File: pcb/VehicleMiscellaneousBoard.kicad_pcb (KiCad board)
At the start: 4 copper layers, 50 x 50 mm, 5 parts, among them J1 Conn_02x05_Top_Bottom, U1 OpenMV H7+, U2 Seeed_Studio_XIAO-ESP32-S3-Se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

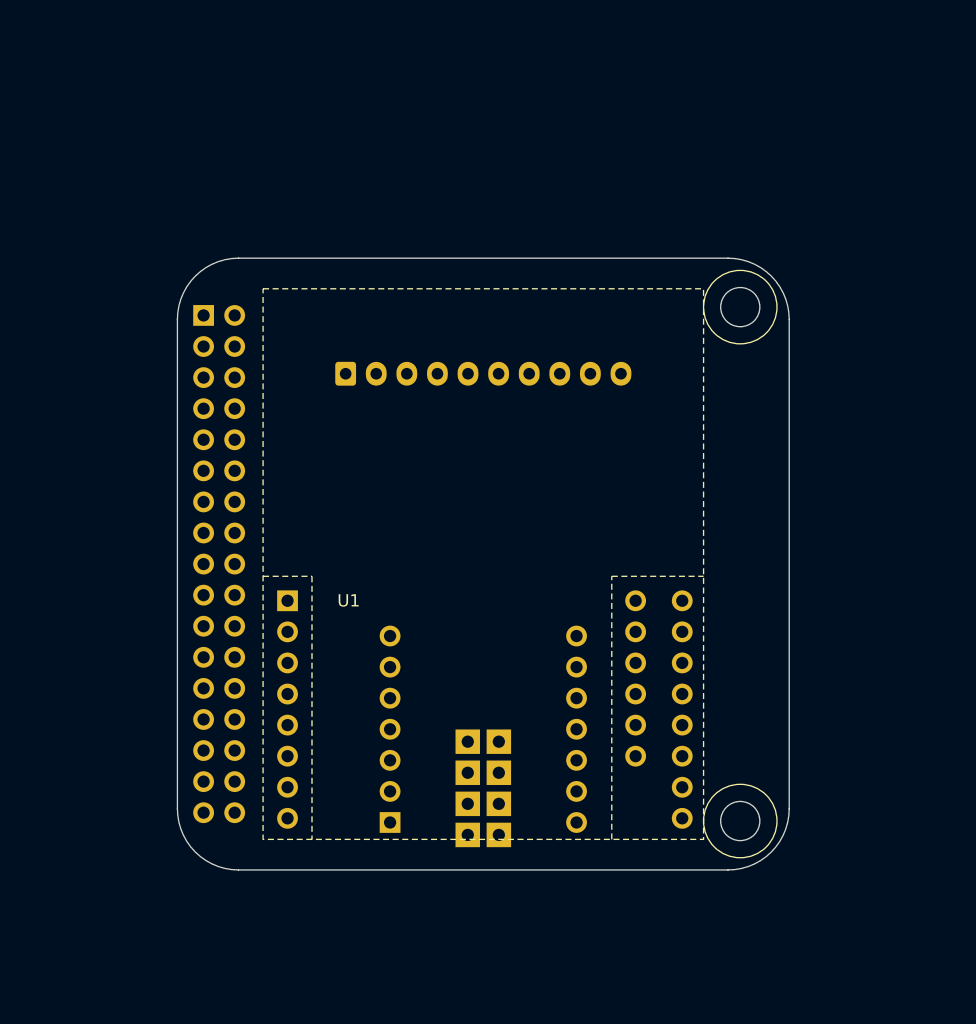
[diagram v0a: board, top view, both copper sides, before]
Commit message: Routed `VehicleMiscellaneousBoard`.
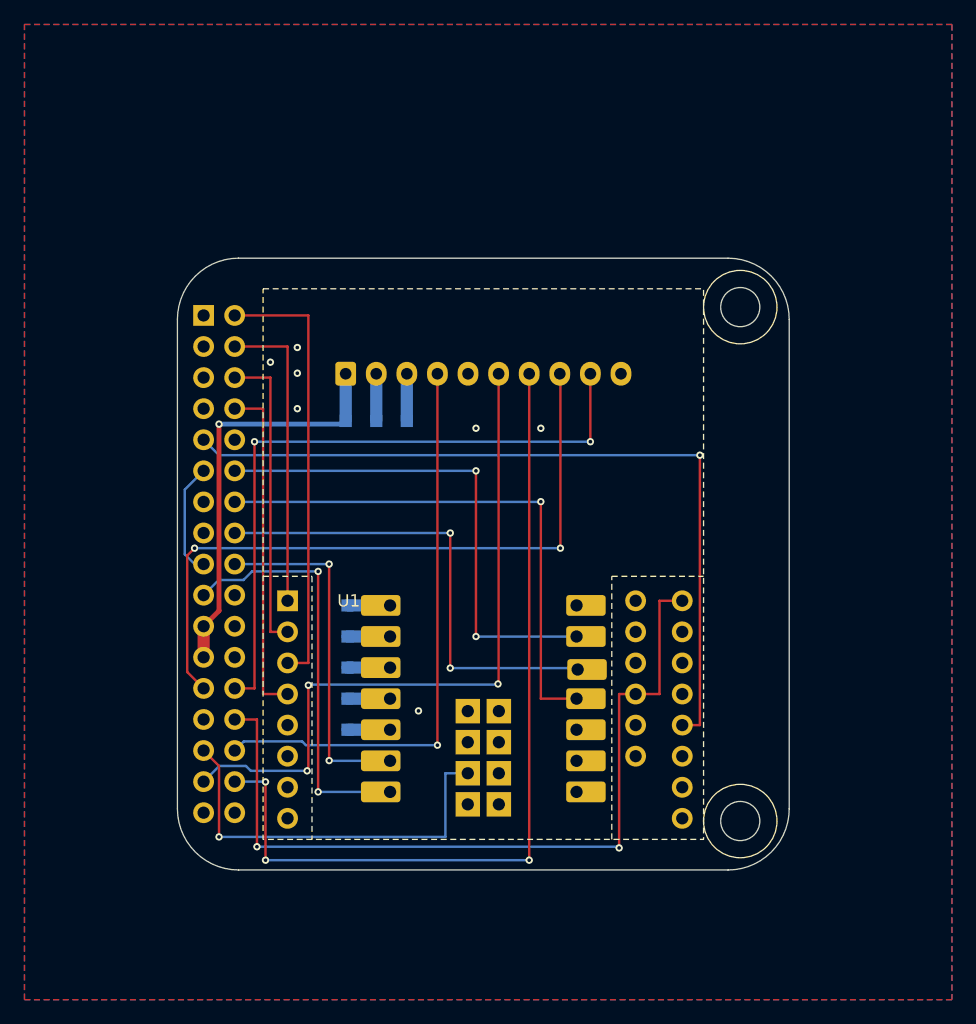
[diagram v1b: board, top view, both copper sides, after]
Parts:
- added TP1: TestPoint, TestPoint:TestPoint_Pad_1.0x1.0mm, B.Cu at (141.2, 88.3)
- added TP10: TestPoint, TestPoint:TestPoint_Pad_1.0x1.0mm, B.Cu at (138.9, 103.4)
- added TP2: TestPoint, TestPoint:TestPoint_Pad_1.0x1.0mm, B.Cu at (143.8, 88.3)
- added TP3: TestPoint, TestPoint:TestPoint_Pad_1.0x1.0mm, B.Cu at (138.8, 88.3)
- added TP6: TestPoint, TestPoint:TestPoint_Pad_1.0x1.0mm, B.Cu at (138.9, 113.5)
- added TP7: TestPoint, TestPoint:TestPoint_Pad_1.0x1.0mm, B.Cu at (138.9, 111.0)
- added TP8: TestPoint, TestPoint:TestPoint_Pad_1.0x1.0mm, B.Cu at (138.9, 108.5)
- added TP9: TestPoint, TestPoint:TestPoint_Pad_1.0x1.0mm, B.Cu at (138.9, 105.9)
- moved U2 2.50 mm to (150.0, 111.0)
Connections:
- J1 pad 1: unconnected-(J1-Pin_1-Pad1) -> +5V
- J1 pad 2: unconnected-(J1-Pin_2-Pad2) -> Net-(J1-Pin_2)
- J1 pad 3: unconnected-(J1-Pin_3-Pad3) -> Net-(J1-Pin_3)
- J1 pad 4: unconnected-(J1-Pin_4-Pad4) -> vn100_sync_out
- J1 pad 5: unconnected-(J1-Pin_5-Pad5) -> GND
- J1 pad 6: unconnected-(J1-Pin_6-Pad6) -> vn100_tare_restore
- J1 pad 7: unconnected-(J1-Pin_7-Pad7) -> vn100_sync_in
- J1 pad 8: unconnected-(J1-Pin_8-Pad8) -> vn100_uart_tx
- J1 pad 9: unconnected-(J1-Pin_9-Pad9) -> vn100_uart_rx
- J6 pad 12: ESP32_SPI_CLOCK -> esp32_spi_clock
- J6 pad 14: ESP32_SPI_MOSI -> esp32_spi_mosi
- J6 pad 16: ESP32_SPI_MISO -> esp32_spi_miso
- J6 pad 18: ESP32_SPI_NSS -> esp32_spi_nss
- J6 pad 19: unconnected-(J6-spi_ready_B-Pad19) -> esp32_spi_ready
- J6 pad 2: OPENMV_SPI_CLOCK -> openmv_spi_clock
- J6 pad 20: unconnected-(J6-GND-Pad20) -> GND
- J6 pad 21: unconnected-(J6-+5V-Pad21) -> +5V
- J6 pad 23: unconnected-(J6-+5V-Pad23) -> +5V
- J6 pad 25: unconnected-(J6-uart_tx_A-Pad25) -> vn100_uart_tx
- J6 pad 26: unconnected-(J6-uart_tx_B-Pad26) -> vn100_uart_rx
- J6 pad 28: OPENMV_RESET -> openmv_reset
- J6 pad 29: ESP32_RESET -> esp32_reset
- J6 pad 30: unconnected-(J6-general_purpose_C-Pad30) -> vn100_sync_out
- J6 pad 31: unconnected-(J6-general_purpose_D-Pad31) -> vn100_tare_restore
- J6 pad 32: unconnected-(J6-NC-Pad32) -> vn100_sync_in
- J6 pad 4: OPENMV_SPI_MOSI -> openmv_spi_mosi
- J6 pad 6: OPENMV_SPI_MISO -> openmv_spi_miso
- J6 pad 8: OPENMV_SPI_NSS -> openmv_spi_nss
- J6 pad 9: OPENMV_SPI_READY -> openmv_spi_ready
- U1 pad NRST: unconnected-(U1-PadNRST) -> openmv_reset
- U1 pad PB12: unconnected-(U1-PadPB12) -> openmv_spi_nss
- U1 pad PB13: unconnected-(U1-PadPB13) -> openmv_spi_clock
- U1 pad PB14: unconnected-(U1-PadPB14) -> openmv_spi_miso
- U1 pad PB15: unconnected-(U1-PadPB15) -> openmv_spi_mosi
- U1 pad PD13: unconnected-(U1-PadPD13) -> openmv_spi_ready
- U2 pad D0: unconnected-(U2-PadD0) -> esp32_spi_ready
- U2 pad D1: unconnected-(U2-PadD1) -> esp32_spi_nss
- U2 pad D10: unconnected-(U2-PadD10) -> esp32_spi_mosi
- U2 pad D2: unconnected-(U2-PadD2) -> Net-(TP6-Pad1)
- U2 pad D3: unconnected-(U2-PadD3) -> Net-(TP7-Pad1)
- U2 pad D4: unconnected-(U2-PadD4) -> Net-(TP8-Pad1)
- U2 pad D5: unconnected-(U2-PadD5) -> Net-(TP9-Pad1)
- U2 pad D6: unconnected-(U2-PadD6) -> Net-(TP10-Pad1)
- U2 pad D8: unconnected-(U2-PadD8) -> esp32_spi_clock
- U2 pad D9: unconnected-(U2-PadD9) -> esp32_spi_miso
- U2 pad EN: unconnected-(U2-PadEN) -> esp32_reset
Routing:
- net vn100_sync_in: track 0.00 -> 70.2 mm, vias 0 -> 3
- net openmv_reset: track 0.00 -> 67.3 mm, vias 0 -> 2
- net openmv_spi_ready: track 0.00 -> 64.6 mm, vias 0 -> 1
- net vn100_tare_restore: track 0.00 -> 57.1 mm, vias 0 -> 3
- net vn100_uart_tx: track 0.00 -> 56.4 mm, vias 0 -> 2
- net vn100_uart_rx: track 0.00 -> 54.8 mm, vias 0 -> 2
- net vn100_sync_out: track 0.00 -> 47.4 mm, vias 0 -> 1
- net esp32_spi_mosi: track 0.00 -> 44.0 mm, vias 0 -> 1
- net GND: track 0.00 -> 43.9 mm
- net esp32_spi_clock: track 0.00 -> 41.5 mm, vias 0 -> 2
- net esp32_spi_miso: track 0.00 -> 39.1 mm, vias 0 -> 2
- net openmv_spi_clock: track 0.00 -> 36.1 mm
- net esp32_spi_ready: track 0.00 -> 34.1 mm, vias 0 -> 2
- net +5V: track 0.00 -> 33.9 mm, vias 0 -> 1
- net esp32_reset: track 0.00 -> 33.1 mm, vias 0 -> 1
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- added copper zone on B.Cu, net +3.3V
- added copper zone on F.Cu, net +3.3V
- added copper zone on In1.Cu, net GND
- added copper zone on In2.Cu, net GND

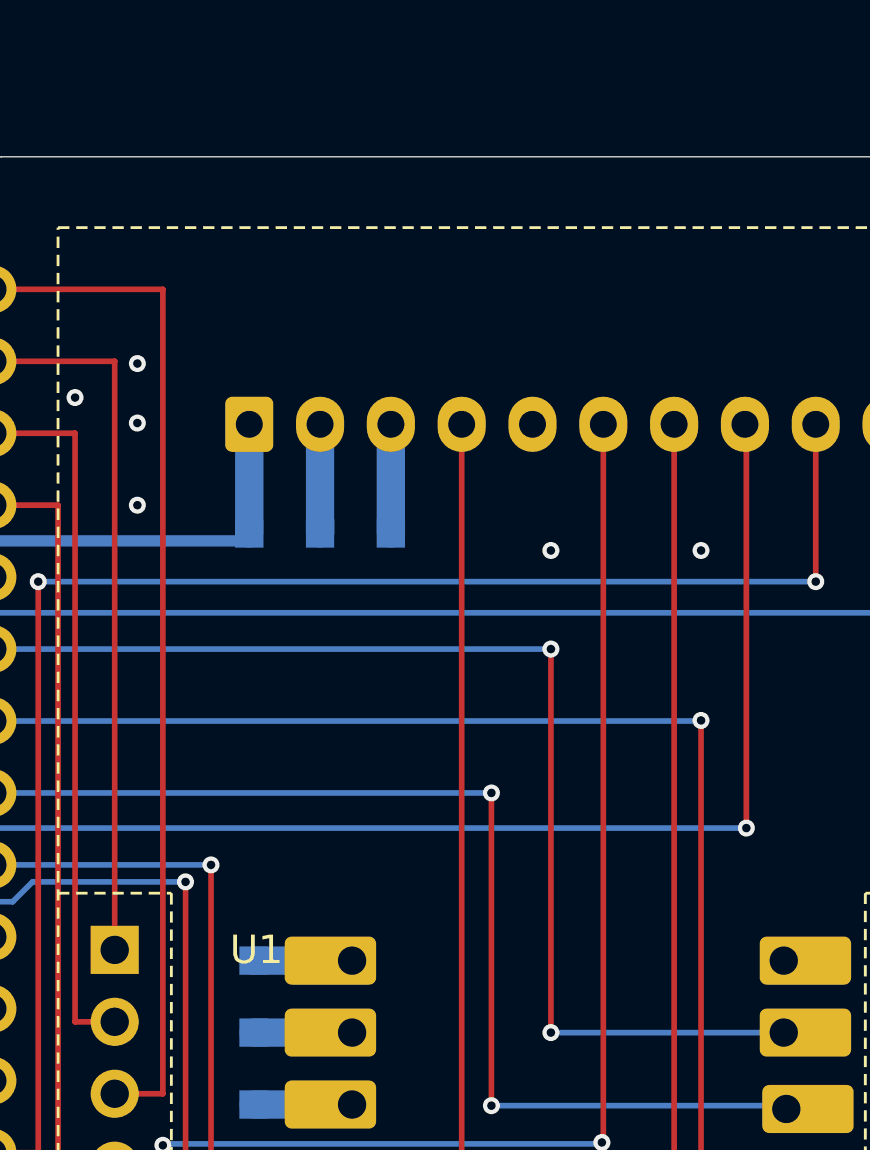
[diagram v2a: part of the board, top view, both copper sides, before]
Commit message: Added PCB name for `VehicleMiscellaneousBoard`.
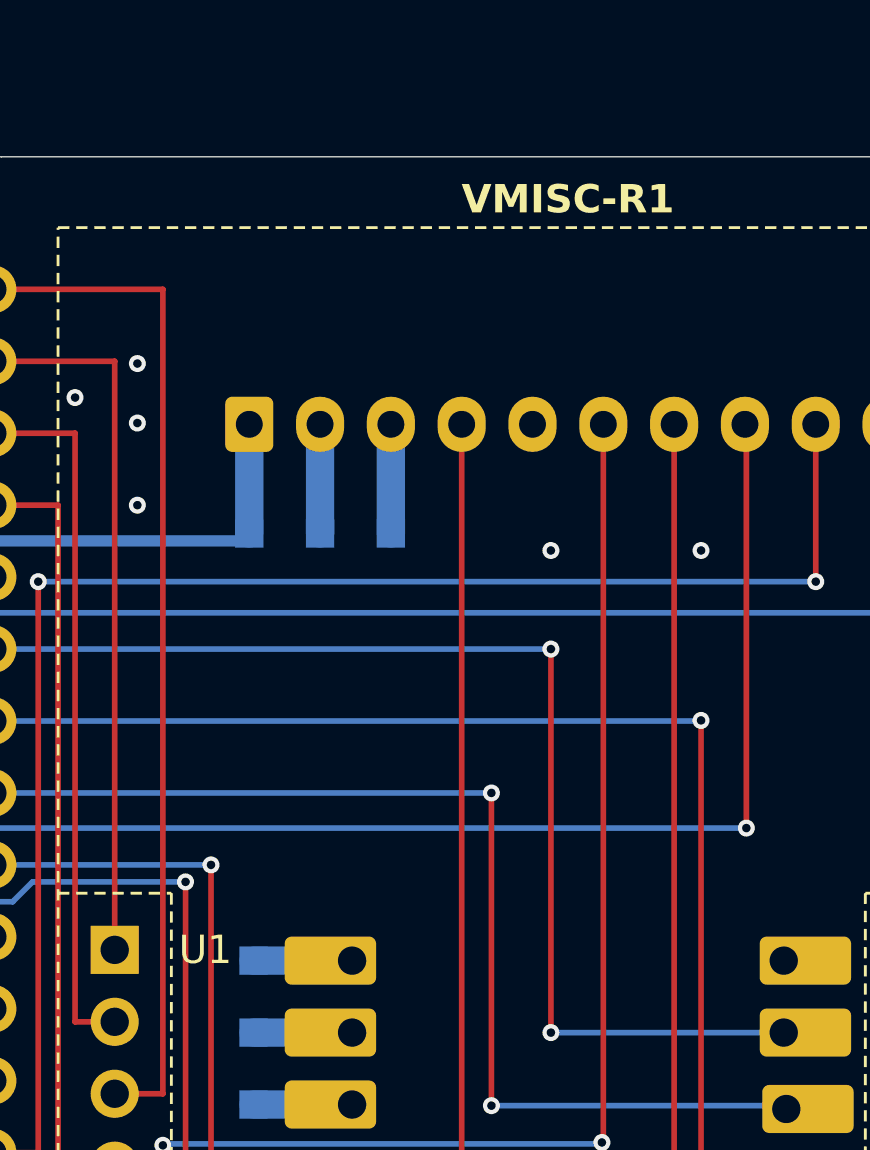
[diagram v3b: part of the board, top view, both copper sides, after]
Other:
- board text added: "VMISC-R1"
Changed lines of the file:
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@@
 		(descr "OpenMV Cam H7 Plus")
 		(property "Reference" "U1"
-			(at 5 0 0)
+			(at 3.2 0 0)
 			(unlocked yes)
 			(layer "F.SilkS")
@@
 		(embedded_fonts no)
 	)
+	(gr_text "VMISC-R1"
+		(at 150 76.5 0)
+		(layer "F.SilkS" knockout)
+		(effects
+			(font
+				(size 1 1)
+				(thickness 0.2)
+				(bold yes)
+			)
+		)
+	)
 	(segment

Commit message: Made schematic symbol of vehicle stack connector match up with the footprint.
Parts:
- renumbered J6 to J1, J1 to J2, TP6 to TP1, TP7 to TP2, TP8 to TP3, TP9 to TP4, TP10 to TP5, TP1 to TP6, TP2 to TP7, TP3 to TP8
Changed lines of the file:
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@@
 	(net 23 "unconnected-(U2-PadMTDI)")
 	(net 24 "unconnected-(U2-PadMTMS)")
-	(net 25 "Net-(TP6-Pad1)")
+	(net 25 "unconnected-(J1-NC-Pad33)")
 	(net 26 "unconnected-(U2-PadD-)")
 	(net 27 "unconnected-(U2-Pad+5V)")
 	(net 28 "unconnected-(U2-PadMTDO)")
-	(net 29 "unconnected-(J1-Pin_10-Pad10)")
-	(net 30 "Net-(TP7-Pad1)")
-	(net 31 "Net-(TP8-Pad1)")
-	(net 32 "Net-(TP9-Pad1)")
-	(net 33 "Net-(TP10-Pad1)")
-	(net 34 "unconnected-(J6-NC-Pad33)")
+	(net 29 "unconnected-(J1-NC-Pad34)")
+	(net 30 "Net-(J2-Pin_2)")
+	(net 31 "Net-(J2-Pin_3)")
+	(net 32 "unconnected-(J2-Pin_10-Pad10)")
+	(net 33 "Net-(TP1-Pad1)")
+	(net 34 "Net-(TP2-Pad1)")
 	(net 35 "unconnected-(U1-PadPD12)")
 	(net 36 "unconnected-(U1-PadPA5)")
 	(net 37 "unconnected-(U1-PadPB11)")
 	(net 38 "unconnected-(U1-PadPG3)")
-	(net 39 "unconnected-(J6-NC-Pad34)")
+	(net 39 "Net-(TP3-Pad1)")
 	(net 40 "unconnected-(U1-PadPB10)")
 	(net 41 "unconnected-(U2-PadD7)")
-	(net 42 "Net-(J1-Pin_2)")
+	(net 42 "Net-(TP4-Pad1)")
 	(net 43 "vn100_sync_in")
 	(net 44 "vn100_sync_out")
 	(net 45 "vn100_tare_restore")
 	(net 46 "+5V")
-	(net 47 "Net-(J1-Pin_3)")
+	(net 47 "Net-(TP5-Pad1)")
 	(net 48 "vn100_uart_rx")
 	(net 49 "vn100_uart_tx")
@@
 		(layer "F.Cu")
 		(at 150 100)
-		(property "Reference" "J6"
+		(property "Reference" "J1"
 			(at 0 -0.5 0)
 			(unlocked yes)
@@
 			(layers "*.Cu" "*.Mask")
 			(remove_unused_layers no)
-			(net 34 "unconnected-(J6-NC-Pad33)")
+			(net 25 "unconnected-(J1-NC-Pad33)")
 			(pinfunction "NC")
 			(pintype "passive+no_connect")
@@
 			(layers "*.Cu" "*.Mask")
 			(remove_unused_layers no)
-			(net 39 "unconnected-(J6-NC-Pad34)")
+			(net 29 "unconnected-(J1-NC-Pad34)")
 			(pinfunction "NC")
 			(pintype "passive+no_connect")
@@
 		(descr "SMD rectangular pad as test Point, square 1.0mm side length")
 		(tags "test point SMD pad rectangle square")
-		(property "Reference" "TP6"
+		(property "Reference" "TP1"
 			(at 0 1.448 0)
 			(layer "B.SilkS")
@@
 			(size 1 1)
 			(layers "B.Cu" "B.Mask")
-			(net 25 "Net-(TP6-Pad1)")
+			(net 33 "Net-(TP1-Pad1)")
 			(pinfunction "1")
 			(pintype "passive")
@@
 		(descr "SMD rectangular pad as test Point, square 1.0mm side length")
 		(tags "test point SMD pad rectangle square")
-		(property "Reference" "TP2"
+		(property "Reference" "TP7"
 			(at 0 1.448 0)
 			(layer "B.SilkS")
@@
 			(size 1 1)
 			(layers "B.Cu" "B.Mask")
-			(net 47 "Net-(J1-Pin_3)")
+			(net 31 "Net-(J2-Pin_3)")
 			(pinfunction "1")
 			(pintype "passive")
@@
 		(descr "SMD rectangular pad as test Point, square 1.0mm side length")
 		(tags "test point SMD pad rectangle square")
-		(property "Reference" "TP10"
+		(property "Reference" "TP5"
 			(at 0 1.448 0)
 			(layer "B.SilkS")
@@
 			(size 1 1)
 			(layers "B.Cu" "B.Mask")
-			(net 33 "Net-(TP10-Pad1)")
+			(net 47 "Net-(TP5-Pad1)")
 			(pinfunction "1")
 			(pintype "passive")
@@
 		(descr "SMD rectangular pad as test Point, square 1.0mm side length")
 		(tags "test point SMD pad rectangle square")
-		(property "Reference" "TP8"
+		(property "Reference" "TP3"
 			(at 0 1.448 0)
 			(layer "B.SilkS")
@@
 			(size 1 1)
 			(layers "B.Cu" "B.Mask")
-			(net 31 "Net-(TP8-Pad1)")
+			(net 39 "Net-(TP3-Pad1)")
 			(pinfunction "1")
 			(pintype "passive")
@@
 		(descr "JST XH series connector, S10B-XH-A (http://www.jst-mfg.com/product/pdf/eng/eXH.pdf), generated with kicad-footprint-generator")
 		(tags "connector JST XH horizontal")
-		(property "Reference" "J1"
+		(property "Reference" "J2"
 			(at 11.25 3.51 180)
 			(layer "B.SilkS")
@@
 			(layers "*.Cu" "*.Mask")
 			(remove_unused_layers no)
-			(net 42 "Net-(J1-Pin_2)")
+			(net 30 "Net-(J2-Pin_2)")
 			(pinfunction "Pin_2")
 			(pintype "passive")
@@
 			(layers "*.Cu" "*.Mask")
 			(remove_unused_layers no)
-			(net 47 "Net-(J1-Pin_3)")
+			(net 31 "Net-(J2-Pin_3)")
 			(pinfunction "Pin_3")
 			(pintype "passive")
@@
 			(layers "*.Cu" "*.Mask")
 			(remove_unused_layers no)
-			(net 29 "unconnected-(J1-Pin_10-Pad10)")
+			(net 32 "unconnected-(J2-Pin_10-Pad10)")
 			(pinfunction "Pin_10")
 			(pintype "passive+no_connect")
@@
 		(descr "SMD rectangular pad as test Point, square 1.0mm side length")
 		(tags "test point SMD pad rectangle square")
-		(property "Reference" "TP1"
+		(property "Reference" "TP6"
 			(at 0 1.448 0)
 			(layer "B.SilkS")
@@
 			(size 1 1)
 			(layers "B.Cu" "B.Mask")
-			(net 42 "Net-(J1-Pin_2)")
+			(net 30 "Net-(J2-Pin_2)")
 			(pinfunction "1")
 			(pintype "passive")
@@
 		(descr "SMD rectangular pad as test Point, square 1.0mm side length")
 		(tags "test point SMD pad rectangle square")
-		(property "Reference" "TP3"
+		(property "Reference" "TP8"
 			(at 0 1.448 0)
 			(layer "B.SilkS")
@@
 			(remove_unused_layers no)
 			(roundrect_rratio 0.1470588235)
-			(net 25 "Net-(TP6-Pad1)")
+			(net 33 "Net-(TP1-Pad1)")
 			(pinfunction "D2")
 			(pintype "passive")
@@
 			(remove_unused_layers no)
 			(roundrect_rratio 0.1470588235)
-			(net 30 "Net-(TP7-Pad1)")
+			(net 34 "Net-(TP2-Pad1)")
 			(pinfunction "D3")
 			(pintype "passive")
@@
 			(remove_unused_layers no)
 			(roundrect_rratio 0.1470588235)
-			(net 31 "Net-(TP8-Pad1)")
+			(net 39 "Net-(TP3-Pad1)")
 			(pinfunction "D4")
 			(pintype "passive")
@@
 			(remove_unused_layers no)
 			(roundrect_rratio 0.1470588235)
-			(net 32 "Net-(TP9-Pad1)")
+			(net 42 "Net-(TP4-Pad1)")
 			(pinfunction "D5")
 			(pintype "passive")
@@
 			(remove_unused_layers no)
 			(roundrect_rratio 0.1470588235)
-			(net 33 "Net-(TP10-Pad1)")
+			(net 47 "Net-(TP5-Pad1)")
 			(pinfunction "D6")
 			(pintype "passive")
@@
 		(descr "SMD rectangular pad as test Point, square 1.0mm side length")
 		(tags "test point SMD pad rectangle square")
-		(property "Reference" "TP7"
+		(property "Reference" "TP2"
 			(at 0 1.448 0)
 			(layer "B.SilkS")
@@
 			(size 1 1)
 			(layers "B.Cu" "B.Mask")
-			(net 30 "Net-(TP7-Pad1)")
+			(net 34 "Net-(TP2-Pad1)")
 			(pinfunction "1")
 			(pintype "passive")
@@
 		(descr "SMD rectangular pad as test Point, square 1.0mm side length")
 		(tags "test point SMD pad rectangle square")
-		(property "Reference" "TP9"
+		(property "Reference" "TP4"
 			(at 0 1.448 0)
 			(layer "B.SilkS")
@@
 			(size 1 1)
 			(layers "B.Cu" "B.Mask")
-			(net 32 "Net-(TP9-Pad1)")
+			(net 42 "Net-(TP4-Pad1)")
 			(pinfunction "1")
 			(pintype "passive")
@@
 	)
 	(segment
-		(start 138.9 113.54)
-		(end 142.38 113.54)
+		(start 141.25 84.445)
+		(end 141.25 88.3)
 		(width 1)
 		(layer "B.Cu")
-		(net 25)
+		(net 30)
 	)
 	(segment
-		(start 138.9 111)
-		(end 142.38 111)
+		(start 143.75 84.445)
+		(end 143.75 88.3)
 		(width 1)
 		(layer "B.Cu")
-		(net 30)
+		(net 31)
 	)
 	(segment
-		(start 138.9 108.46)
-		(end 142.38 108.46)
+		(start 138.9 113.54)
+		(end 142.38 113.54)
 		(width 1)
 		(layer "B.Cu")
-		(net 31)
+		(net 33)
 	)
 	(segment
-		(start 138.9 105.92)
-		(end 142.38 105.92)
+		(start 138.9 111)
+		(end 142.38 111)
 		(width 1)
 		(layer "B.Cu")
-		(net 32)
+		(net 34)
 	)
 	(segment
-		(start 138.9 103.38)
-		(end 142.38 103.38)
+		(start 138.9 108.46)
+		(end 142.38 108.46)
 		(width 1)
 		(layer "B.Cu")
-		(net 33)
+		(net 39)
 	)
 	(segment
-		(start 141.25 84.445)
-		(end 141.25 88.3)
+		(start 138.9 105.92)
+		(end 142.38 105.92)
 		(width 1)
 		(layer "B.Cu")
@@
 	)
 	(segment
-		(start 143.75 84.445)
-		(end 143.75 88.3)
+		(start 138.9 103.38)
+		(end 142.38 103.38)
 		(width 1)
 		(layer "B.Cu")
